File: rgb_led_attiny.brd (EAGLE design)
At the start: 57.6 x 55.8 mm, 14 parts, among them IC1 ATTINY45-20PU, IC2 MC7805BTG, Q1 IRF540NPBF, Q2 IRF540NPBF, Q3 IRF540NPBF

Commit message: Premier routage
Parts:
- moved C2 17.9 mm to (5.71, 44.5), turned to 180 degrees
- moved R1 10.8 mm to (37.1, 40.6)
- moved R3 10.0 mm to (37.1, 13.3)
- moved IC2 9.09 mm to (12.7, 38.7), turned to 90 degrees
- moved Q1 9.09 mm to (23.4, 46.8)
- moved Q2 8.98 mm to (23.6, 30.4)
- moved Q3 8.91 mm to (23.9, 14.1)
- moved C1 8.35 mm to (5.71, 38.1), turned to 180 degrees
- moved JP1 7.01 mm to (4.45, 32.4)
- moved JP4 5.24 mm to (47.1, 11.4)
- moved JP2 5.12 mm to (47.1, 41.3)
- moved JP3 5.12 mm to (47.1, 27.3)
- moved R2 4.49 mm to (42.2, 27.3)
- moved IC1 1.27 mm to (15.2, 16.5)
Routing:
- net VCC: track 0.00 -> 139.0 mm
- net PWM_R: track 0.00 -> 28.6 mm
- net N$2: track 0.00 -> 24.5 mm
- net N$3: track 0.00 -> 18.4 mm
- net N$6: track 0.00 -> 16.6 mm
- net N$7: track 0.00 -> 15.3 mm
- net PWM_G: track 0.00 -> 14.9 mm
- net N$4: track 0.00 -> 12.4 mm
- net N$1: track 0.00 -> 11.5 mm
- net PWM_B: track 0.00 -> 9.63 mm
- net N$5: track 0.00 -> 8.41 mm
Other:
- board size 57.6 x 55.8 mm -> 53.1 x 50.7 mm

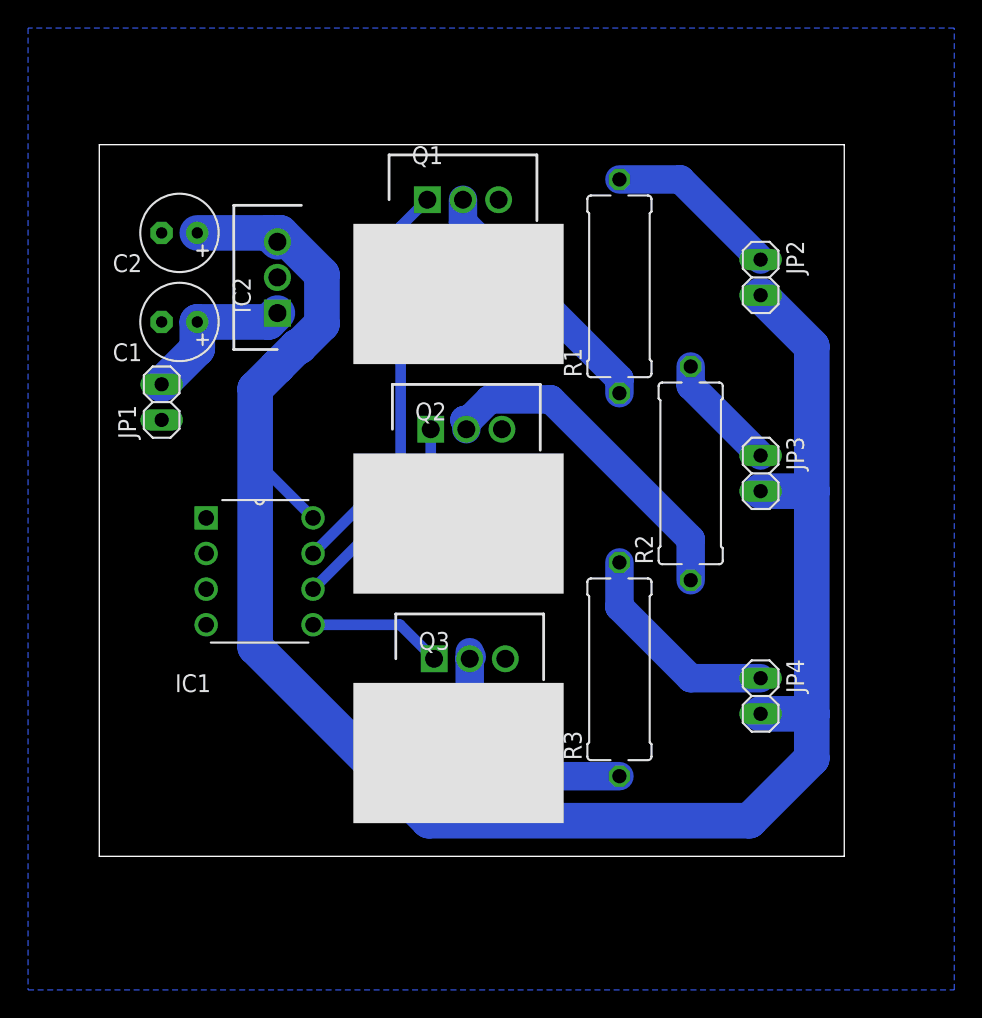
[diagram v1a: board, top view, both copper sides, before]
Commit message: Deuxième routage, plus compact avecles resistances en vertical. Ajout de pull-down sur le gate des MOSFETs
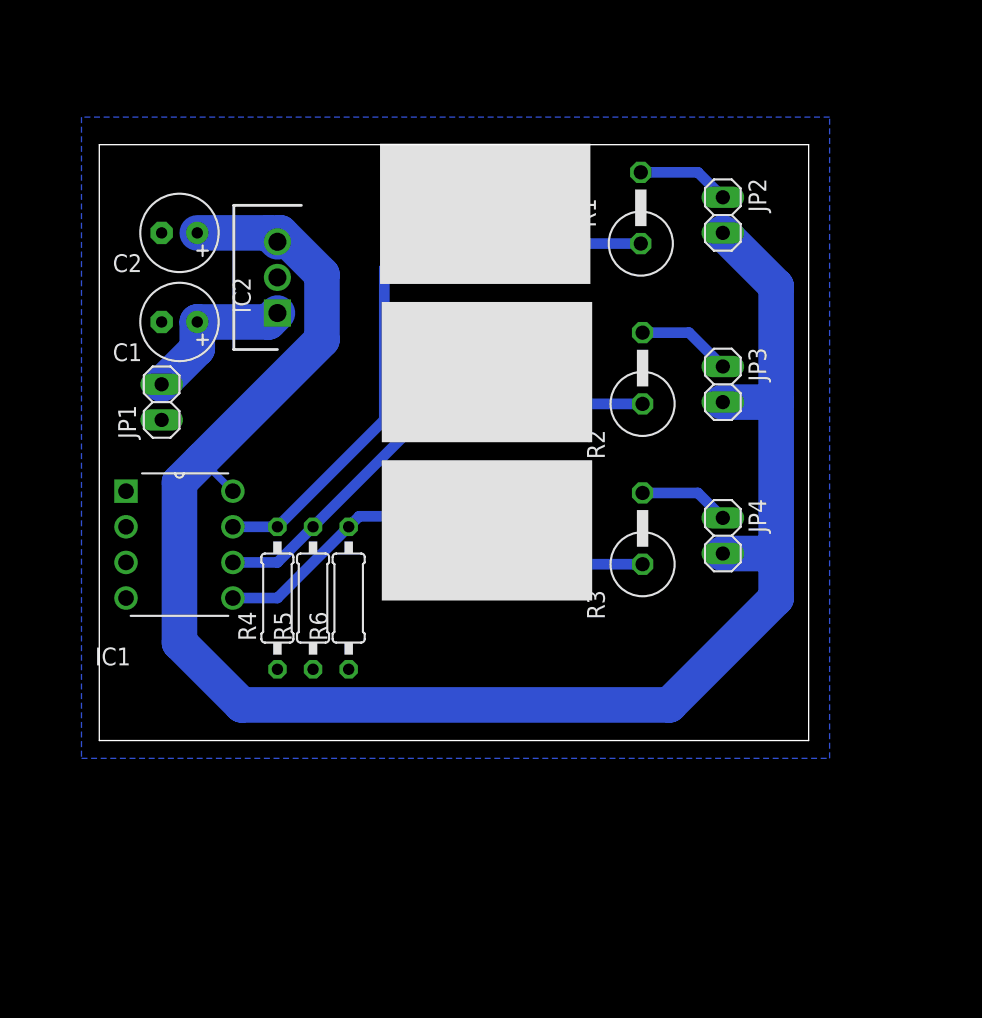
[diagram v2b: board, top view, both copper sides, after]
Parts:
- added R4, R5, R6: (no value), rcl:0207/10
- R1, R2, R3: device rcl:P0613/15 -> rcl:P0613V
- moved JP4 11.7 mm to (44.5, 22.9)
- moved Q3 10.3 mm to (25.3, 24.2)
- moved R3 10.2 mm to (38.7, 23.4)
- moved R2 8.24 mm to (38.7, 34.8)
- moved JP3 6.90 mm to (44.5, 33.7)
- moved IC1 6.02 mm to (9.53, 18.4)
- moved R1 5.79 mm to (38.6, 46.2)
- moved Q2 5.27 mm to (25.0, 35.5)
- moved JP2 5.20 mm to (44.5, 45.7)
- moved Q1 1.91 mm to (25.3, 46.8)
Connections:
- net GND: now also R4.1, R5.1, R6.1
- net PWM_B: now also R6.2
- net PWM_G: now also R5.2
- net PWM_R: now also R4.2
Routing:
- net N$2: track 24.5 -> 12.5 mm
- net VCC: track 139.0 -> 127.4 mm
- net N$7: track 15.3 -> 6.46 mm
- net PWM_B: track 9.63 -> 18.2 mm
- net PWM_G: track 14.9 -> 22.9 mm
- net N$3: track 18.4 -> 12.1 mm
- net N$4: track 12.4 -> 6.59 mm
- net N$6: track 16.6 -> 12.3 mm
- net PWM_R: track 28.6 -> 31.8 mm
- net N$5: track 8.41 -> 6.72 mm
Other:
- board size 53.1 x 50.7 mm -> 50.6 x 42.5 mm

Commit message: Encore un peu de gain de place
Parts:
- moved R4 3.81 mm to (12.7, 22.2)
- moved R5 3.81 mm to (15.2, 22.2)
- moved R6 3.81 mm to (17.8, 22.2)
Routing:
- net VCC: track 127.4 -> 121.2 mm
- net PWM_B: track 18.2 -> 21.1 mm
- net PWM_R: track 31.8 -> 29.9 mm
- net PWM_G: track 22.9 -> 21.9 mm
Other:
- board size 50.6 x 42.5 mm -> 50.6 x 38.7 mm
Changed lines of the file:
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@@
 <board>
 <plain>
-<wire x1="0" y1="8.255" x2="50.575" y2="8.255" width="0" layer="20"/>
-<wire x1="50.575" y1="8.255" x2="50.575" y2="50.74" width="0" layer="20"/>
+<wire x1="0" y1="12.065" x2="50.575" y2="12.065" width="0" layer="20"/>
+<wire x1="50.575" y1="12.065" x2="50.575" y2="50.74" width="0" layer="20"/>
 <wire x1="50.575" y1="50.74" x2="0" y2="50.74" width="0" layer="20"/>
-<wire x1="0" y1="50.74" x2="0" y2="8.255" width="0" layer="20"/>
+<wire x1="0" y1="50.74" x2="0" y2="12.065" width="0" layer="20"/>
 <rectangle x1="20.015" y1="40.81" x2="35.015" y2="50.81" layer="21" rot="R180"/>
 <rectangle x1="20.142" y1="29.525" x2="35.142" y2="39.525" layer="21" rot="R180"/>
 <rectangle x1="20.142" y1="18.24" x2="35.142" y2="28.24" layer="21"/>
 <dimension x1="50.575" y1="50.74" x2="0" y2="50.74" x3="25.2875" y3="53.975" textsize="1.778" layer="20" dtype="horizontal"/>
-<dimension x1="0" y1="50.74" x2="0" y2="8.255" x3="-5.08" y3="29.4975" textsize="1.778" layer="20" dtype="horizontal"/>
+<dimension x1="0" y1="50.74" x2="0" y2="12.065" x3="-5.715" y3="31.4025" textsize="1.778" layer="20" dtype="horizontal"/>
 </plain>
 <attributes>
@@
 <attribute name="VALUE" x="39.4472" y="19.05" size="1.27" layer="27" ratio="10" rot="R90"/>
 </element>
-<element name="R4" library="rcl" library_urn="urn:adsk.eagle:library:334" package="0207/10" package3d_urn="urn:adsk.eagle:package:23491/1" value="" x="12.7" y="18.415" smashed="yes" rot="R90">
-<attribute name="NAME" x="11.176" y="15.367" size="1.27" layer="25" ratio="10" rot="R90"/>
-<attribute name="SPICEPREFIX" value="R" x="12.7" y="18.415" size="1.778" layer="27" rot="R90" display="off"/>
-<attribute name="VALUE" x="13.335" y="16.1544" size="1.27" layer="27" ratio="10" rot="R90"/>
-</element>
-<element name="R5" library="rcl" library_urn="urn:adsk.eagle:library:334" package="0207/10" package3d_urn="urn:adsk.eagle:package:23491/1" value="" x="15.24" y="18.415" smashed="yes" rot="R90">
-<attribute name="NAME" x="13.716" y="15.367" size="1.27" layer="25" ratio="10" rot="R90"/>
-<attribute name="SPICEPREFIX" value="R" x="15.24" y="18.415" size="1.778" layer="27" rot="R90" display="off"/>
-<attribute name="VALUE" x="15.875" y="16.1544" size="1.27" layer="27" ratio="10" rot="R90"/>
-</element>
-<element name="R6" library="rcl" library_urn="urn:adsk.eagle:library:334" package="0207/10" package3d_urn="urn:adsk.eagle:package:23491/1" value="" x="17.78" y="18.415" smashed="yes" rot="R90">
-<attribute name="NAME" x="16.256" y="15.367" size="1.27" layer="25" ratio="10" rot="R90"/>
-<attribute name="SPICEPREFIX" value="R" x="17.78" y="18.415" size="1.778" layer="27" rot="R90" display="off"/>
-<attribute name="VALUE" x="18.415" y="16.1544" size="1.27" layer="27" ratio="10" rot="R90"/>
+<element name="R4" library="rcl" library_urn="urn:adsk.eagle:library:334" package="0207/10" package3d_urn="urn:adsk.eagle:package:23491/1" value="" x="12.7" y="22.225" smashed="yes" rot="R90">
+<attribute name="NAME" x="11.176" y="19.177" size="1.27" layer="25" ratio="10" rot="R90"/>
+<attribute name="SPICEPREFIX" value="R" x="12.7" y="22.225" size="1.778" layer="27" rot="R90" display="off"/>
+<attribute name="VALUE" x="13.335" y="19.9644" size="1.27" layer="27" ratio="10" rot="R90"/>
+</element>
+<element name="R5" library="rcl" library_urn="urn:adsk.eagle:library:334" package="0207/10" package3d_urn="urn:adsk.eagle:package:23491/1" value="" x="15.24" y="22.225" smashed="yes" rot="R90">
+<attribute name="NAME" x="13.716" y="19.177" size="1.27" layer="25" ratio="10" rot="R90"/>
+<attribute name="SPICEPREFIX" value="R" x="15.24" y="22.225" size="1.778" layer="27" rot="R90" display="off"/>
+<attribute name="VALUE" x="15.875" y="19.9644" size="1.27" layer="27" ratio="10" rot="R90"/>
+</element>
+<element name="R6" library="rcl" library_urn="urn:adsk.eagle:library:334" package="0207/10" package3d_urn="urn:adsk.eagle:package:23491/1" value="" x="17.78" y="22.225" smashed="yes" rot="R90">
+<attribute name="NAME" x="16.256" y="19.177" size="1.27" layer="25" ratio="10" rot="R90"/>
+<attribute name="SPICEPREFIX" value="R" x="17.78" y="22.225" size="1.778" layer="27" rot="R90" display="off"/>
+<attribute name="VALUE" x="18.415" y="19.9644" size="1.27" layer="27" ratio="10" rot="R90"/>
 </element>
 </elements>
@@
 <wire x1="48.26" y1="40.6476" x2="48.26" y2="32.385" width="2.54" layer="16"/>
 <wire x1="48.26" y1="32.385" x2="48.26" y2="21.59" width="2.54" layer="16"/>
-<wire x1="48.26" y1="21.59" x2="48.26" y2="18.415" width="2.54" layer="16"/>
+<wire x1="48.26" y1="21.59" x2="48.26" y2="20.955" width="2.54" layer="16"/>
 <wire x1="44.4576" y1="21.59" x2="48.26" y2="21.59" width="2.54" layer="16"/>
 <wire x1="44.4576" y1="32.385" x2="48.26" y2="32.385" width="2.54" layer="16"/>
-<wire x1="40.64" y1="10.795" x2="48.26" y2="18.415" width="2.54" layer="16"/>
+<wire x1="41.91" y1="14.605" x2="48.26" y2="20.955" width="2.54" layer="16"/>
 <wire x1="15.875" y1="36.83" x2="7.3025" y2="28.2575" width="2.54" layer="16"/>
 <wire x1="7.3025" y1="28.2575" x2="5.715" y2="26.67" width="2.54" layer="16"/>
-<wire x1="5.715" y1="15.24" x2="10.16" y2="10.795" width="2.54" layer="16"/>
+<wire x1="5.715" y1="17.78" x2="8.89" y2="14.605" width="2.54" layer="16"/>
 <wire x1="15.875" y1="41.47983125" x2="15.875" y2="36.83" width="2.54" layer="16"/>
-<wire x1="5.715" y1="26.67" x2="5.715" y2="15.24" width="2.54" layer="16"/>
-<wire x1="10.16" y1="10.795" x2="40.64" y2="10.795" width="2.54" layer="16"/>
+<wire x1="5.715" y1="26.67" x2="5.715" y2="17.78" width="2.54" layer="16"/>
+<wire x1="8.89" y1="14.605" x2="41.91" y2="14.605" width="2.54" layer="16"/>
 <wire x1="9.525" y1="26.035" x2="7.3025" y2="28.2575" width="0.508" layer="16"/>
 </signal>
@@
 <contactref element="Q3" pad="1"/>
 <contactref element="R6" pad="2"/>
-<wire x1="17.78" y1="23.495" x2="18.53" y2="24.245" width="0.762" layer="16"/>
-<wire x1="18.53" y1="24.245" x2="25.267" y2="24.245" width="0.762" layer="16"/>
-<wire x1="9.525" y1="18.415" x2="12.7" y2="18.415" width="0.762" layer="16"/>
-<wire x1="12.7" y1="18.415" x2="17.78" y2="23.495" width="0.762" layer="16"/>
+<wire x1="9.525" y1="18.415" x2="17.78" y2="26.67" width="0.762" layer="16"/>
+<wire x1="17.78" y1="26.67" x2="17.78" y2="27.305" width="0.762" layer="16"/>
+<wire x1="17.78" y1="27.305" x2="22.207" y2="27.305" width="0.762" layer="16"/>
+<wire x1="22.207" y1="27.305" x2="25.267" y2="24.245" width="0.762" layer="16"/>
 </signal>
 <signal name="PWM_G">
@@
 <contactref element="Q2" pad="1"/>
 <contactref element="R5" pad="2"/>
-<wire x1="15.24" y1="23.495" x2="25.027" y2="33.282" width="0.762" layer="16"/>
-<wire x1="25.027" y1="33.282" x2="25.027" y2="35.53" width="0.762" layer="16"/>
-<wire x1="9.525" y1="20.955" x2="12.7" y2="20.955" width="0.762" layer="16"/>
-<wire x1="12.7" y1="20.955" x2="15.24" y2="23.495" width="0.762" layer="16"/>
+<wire x1="9.525" y1="20.955" x2="15.24" y2="26.67" width="0.762" layer="16"/>
+<wire x1="15.24" y1="26.67" x2="15.24" y2="27.305" width="0.762" layer="16"/>
+<wire x1="15.24" y1="27.305" x2="23.465" y2="35.53" width="0.762" layer="16"/>
+<wire x1="23.465" y1="35.53" x2="25.027" y2="35.53" width="0.762" layer="16"/>
 </signal>
 <signal name="PWM_R">
@@
 <contactref element="Q1" pad="1"/>
 <contactref element="R4" pad="2"/>
-<wire x1="9.525" y1="23.495" x2="12.7" y2="23.495" width="0.762" layer="16"/>
-<wire x1="12.7" y1="23.495" x2="20.32" y2="31.115" width="0.762" layer="16"/>
-<wire x1="20.32" y1="31.115" x2="20.32" y2="41.91" width="0.762" layer="16"/>
+<wire x1="25.225" y1="46.815" x2="25.295" y2="46.815" width="0.762" layer="16"/>
+<wire x1="9.525" y1="23.495" x2="12.7" y2="26.67" width="0.762" layer="16"/>
+<wire x1="12.7" y1="26.67" x2="12.7" y2="27.305" width="0.762" layer="16"/>
+<wire x1="12.7" y1="27.305" x2="20.32" y2="34.925" width="0.762" layer="16"/>
 <wire x1="20.32" y1="41.91" x2="25.225" y2="46.815" width="0.762" layer="16"/>
-<wire x1="25.225" y1="46.815" x2="25.295" y2="46.815" width="0.762" layer="16"/>
+<wire x1="20.32" y1="34.925" x2="20.32" y2="41.91" width="0.762" layer="16"/>
 </signal>
 <signal name="N$3">
